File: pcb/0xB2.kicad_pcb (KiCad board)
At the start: 2 copper layers, 41.8 x 50.8 mm, 59 parts, among them J10 RGB, J11 serial, J14 Conn_01x02_Female, J15 Conn_01x02_Female, J5 Conn_01x02, J6 Ribbon, J7 Ribbon, J8 trackball, J9 Serial, SW2 SW_Push, SW3 SW_SPST, U1 RP2040, U2 GD25Q80CEIGR, U3 XC6210B332MR-G, Y1 Crystal_GND24

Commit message: version
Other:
- board text added: "0.1c"
- board text removed: "0.1b"
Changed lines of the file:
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@@
     (effects (font (size 0.8 0.8) (thickness 0.15)))
   )
-  (gr_text "0.1b" (at 167.925 113.25) (layer "F.SilkS")
+  (gr_text "0.1c" (at 167.925 113.25) (layer "F.SilkS")
     (effects (font (size 0.8 0.8) (thickness 0.15)))
   )

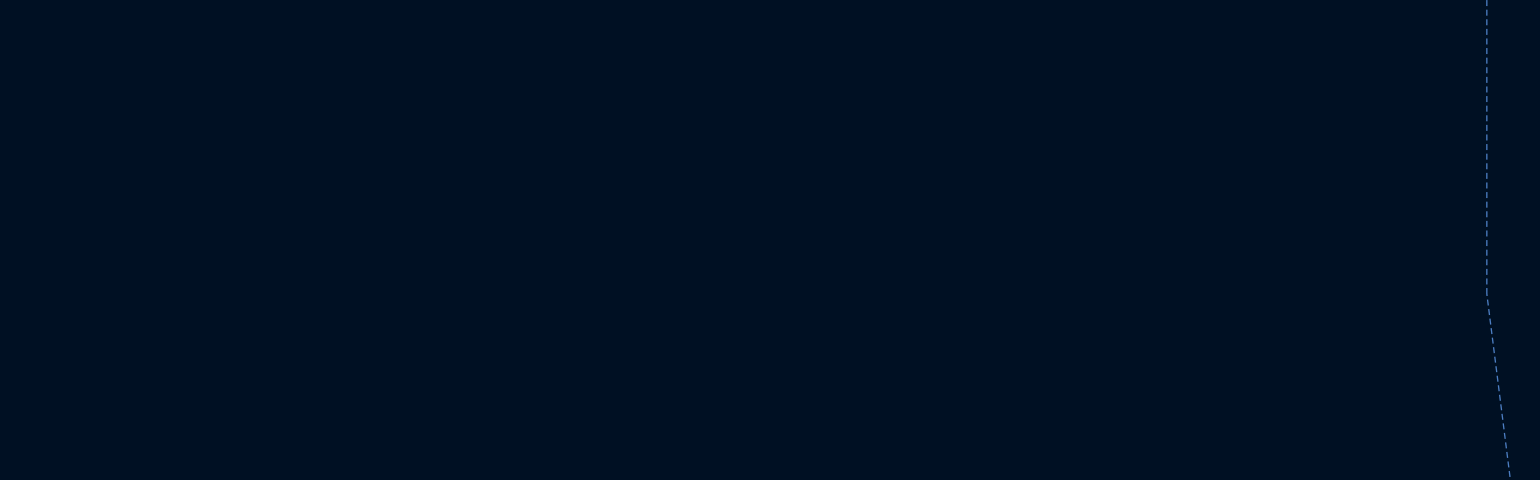
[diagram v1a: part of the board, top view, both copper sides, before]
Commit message: same layout as chris (need to route)
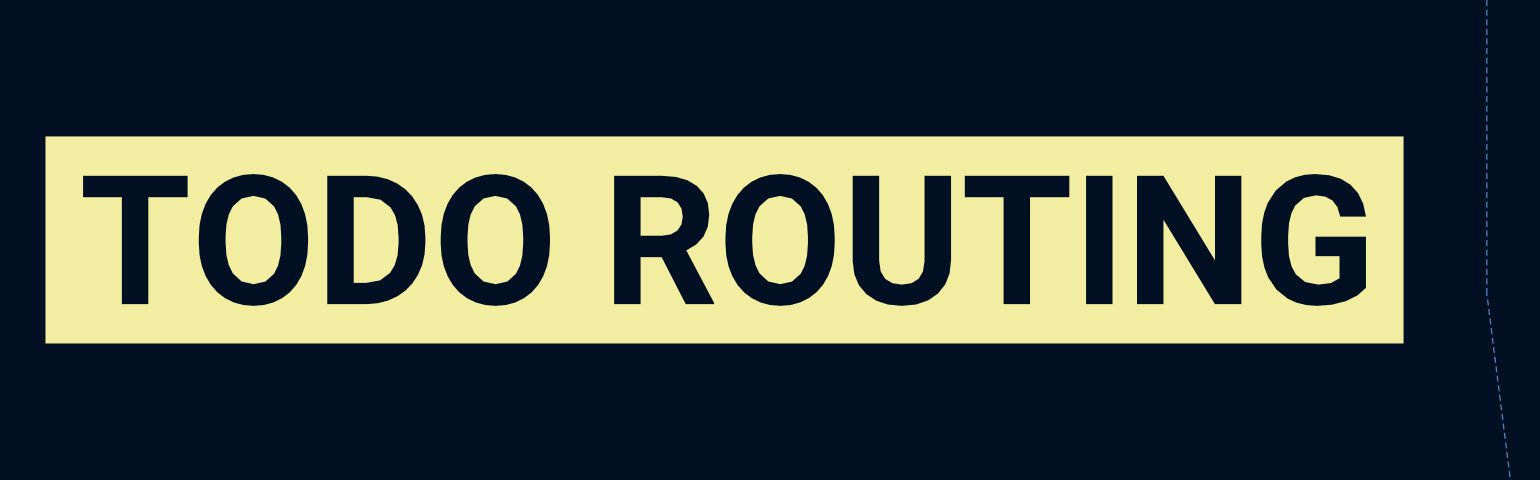
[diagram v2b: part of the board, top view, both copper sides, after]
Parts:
- added kibuzzard-62A08E5A: G***, kibuzzard-62A08E5A, F.Cu at (95.8, 87.8)
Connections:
- net /A0 renamed row2_l
- net /A1 renamed col1_l
- net /A2 renamed col2_l
- net /A3 renamed row1_l
- net /D0 renamed rgb_r
- net /D1 renamed serial_l
- net /D2 renamed sda_l
- net /D21 renamed col3_l
- net /D3 renamed scl_l
- net /D4 renamed row4_l
- net /D5 renamed row3_l
- net /D6 renamed col4_l
- net /D7 renamed col5_l
- net /D8 renamed col6_l
- net /D9 renamed row5_l
- net /MISO renamed miso_l
- net /MOSI renamed mosi_l
- net /SCLK renamed sc_l
- J8 pad 2: /D14 -> ss_l
- U1 pad 18: unconnected-(U1-Pad18) -> split_hand_l
- U1 pad 27: unconnected-(U1-Pad27) -> ss_l
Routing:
- net ss_l: track 0.00 -> 29.2 mm, vias 0 -> 1
- net /D14: track 29.2 -> 0.00 mm, vias 1 -> 0

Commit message: routing
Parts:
- moved D1 13.0 mm to (159.9, 93.3), turned to -90 degrees
- moved R1 12.5 mm to (161.0, 93.3), turned to 90 degrees
- moved C14 0.73 mm to (154.5, 103.6)
- moved R14 0.69 mm to (154.6, 107.0)
- moved C8 0.69 mm to (154.5, 102.5)
- moved C13 0.60 mm to (158.1, 98.7)
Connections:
- R14 pad 1: /D13 -> split_hand_l
- U1 pad 28: /LED -> unconnected-(U1-Pad28)
- U1 pad 30: unconnected-(U1-Pad30) -> /VBUS_DET
- U1 pad 37: /VBUS_DET -> /LED
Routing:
- net split_hand_l: track 0.00 -> 19.4 mm
- net /D13: track 18.9 -> 0.00 mm
- net ss_l: track 29.2 -> 23.8 mm
- net /LED: track 11.4 -> 7.49 mm, vias 0 -> 2
- net /VBUS_DET: track 11.5 -> 14.7 mm
- net +3V3: track 77.3 -> 79.7 mm
- net col3_l: track 17.1 -> 17.9 mm

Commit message: silkscreen
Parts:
- removed kibuzzard-62A08E5A: G***, kibuzzard-62A08E5A
- added G***: LOGO, LOGO, F.Cu at (153.8, 82.0)
- added G***: LOGO, LOGO, B.Cu at (153.8, 82.0)
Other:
- board text added: "0.2"
- board text removed: "0.1c"

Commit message: silkscreen
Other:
- board text added: "GITHUB.COM/BASTARDKB"
- board text added: "Licensed under CERN-OHL-S v2"
- board text added: "RP2040_SHIELD"
- board text removed: "rp2040 shield"
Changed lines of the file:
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@@
   (gr_line (start 169.181051 114.391051) (end 173.011529 114.400074) (layer "Edge.Cuts") (width 0.2))
   (gr_rect (start 156.175 82.325) (end 148.575 75.415) (layer "F.Fab") (width 0.1) (fill none))
+  (gr_text "GITHUB.COM/BASTARDKB" (at 150.396692 108.29) (layer "B.SilkS")
+    (effects (font (size 0.8 0.8) (thickness 0.12)) (justify mirror))
+  )
   (gr_text "R5" (at 149.988524 125.960001 315) (layer "B.SilkS")
     (effects (font (size 0.8 0.8) (thickness 0.15)) (justify mirror))
   )
-  (gr_text "5V" (at 162.880222 102.72 -45) (layer "B.SilkS")
+  (gr_text "5V" (at 163.271294 102.7 -45) (layer "B.SilkS")
     (effects (font (size 0.8 0.8) (thickness 0.15)) (justify mirror))
   )
@@
     (effects (font (size 0.8 0.8) (thickness 0.15)) (justify mirror))
   )
-  (gr_text "GND" (at 163.230408 105.26 -45) (layer "B.SilkS")
+  (gr_text "GND" (at 162.921108 105.24 -45) (layer "B.SilkS")
     (effects (font (size 0.8 0.8) (thickness 0.15)) (justify mirror))
   )
@@
     (effects (font (size 0.8 0.8) (thickness 0.15)) (justify mirror))
   )
-  (gr_text "rp2040 shield" (at 147.74 108.43) (layer "B.SilkS")
-    (effects (font (size 0.8 0.8) (thickness 0.12)) (justify mirror))
-  )
   (gr_text "C6" (at 149.988524 123.420001 315) (layer "B.SilkS")
     (effects (font (size 0.8 0.8) (thickness 0.15)) (justify mirror))
   )
-  (gr_text "DIN" (at 163.082253 107.8 -45) (layer "B.SilkS")
+  (gr_text "DIN" (at 163.069263 107.78 -45) (layer "B.SilkS")
     (effects (font (size 0.8 0.8) (thickness 0.15)) (justify mirror))
+  )
+  (gr_text "Licensed under \nCERN-OHL-S v2" (at 153.63 86.7) (layer "B.SilkS")
+    (effects (font (size 0.8 0.8) (thickness 0.12)) (justify mirror))
   )
   (gr_text "R3" (at 149.988524 115.800001 315) (layer "B.SilkS")
@@
     (effects (font (size 0.8 0.8) (thickness 0.15)))
   )
-  (gr_text "rp2040 shield" (at 147.74 108.4) (layer "F.SilkS")
+  (gr_text "RP2040_SHIELD" (at 147.936692 108.4) (layer "F.SilkS")
     (effects (font (size 0.8 0.8) (thickness 0.12)))
   )
